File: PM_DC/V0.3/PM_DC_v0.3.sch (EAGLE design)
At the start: 49 parts, among them J1 M13PTH-CST-R, J2 M12PTH-CST-R, U2 LMR14030, U3 MP1601GTF-Z, U5 TPS22918

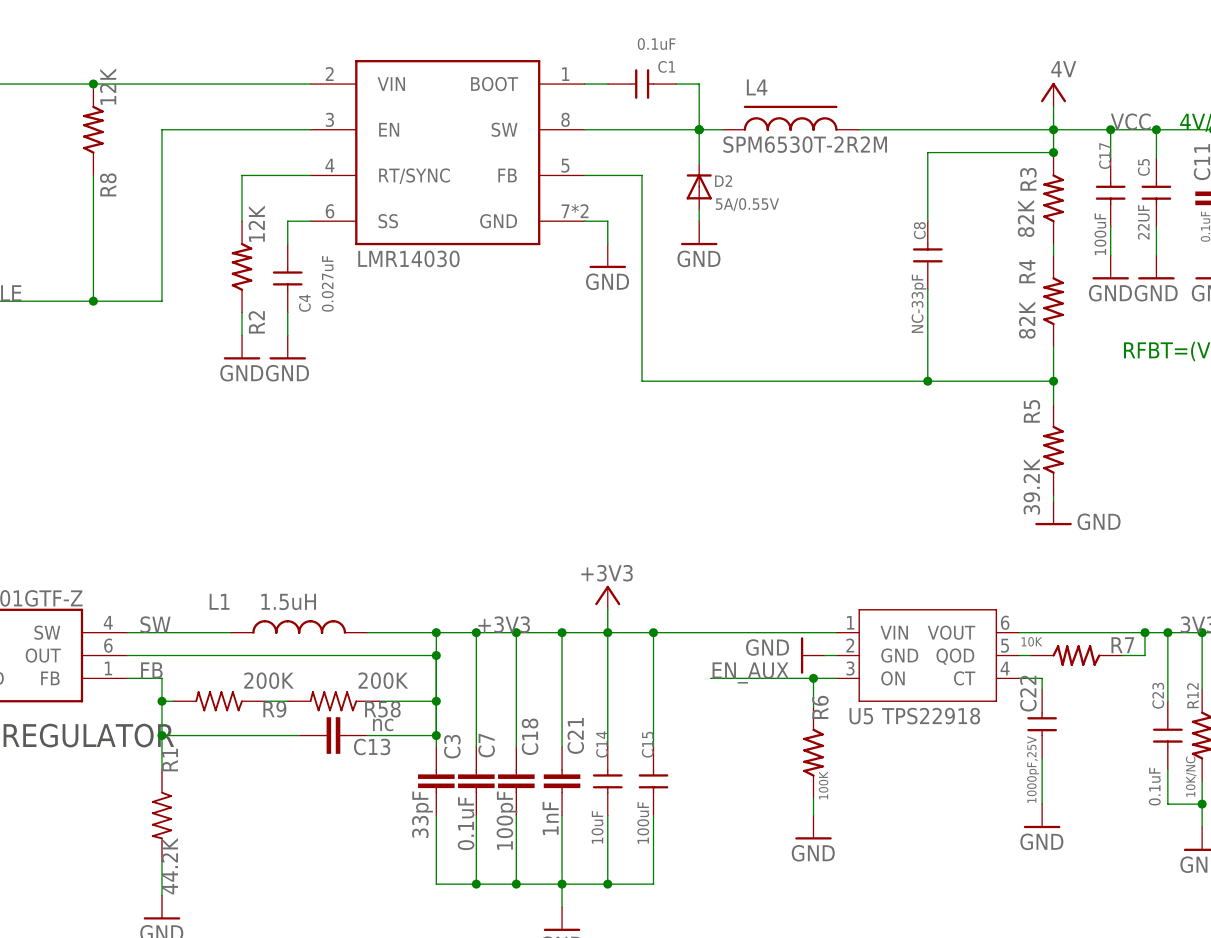
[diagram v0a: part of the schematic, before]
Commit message: update
output gerber for MO DFM
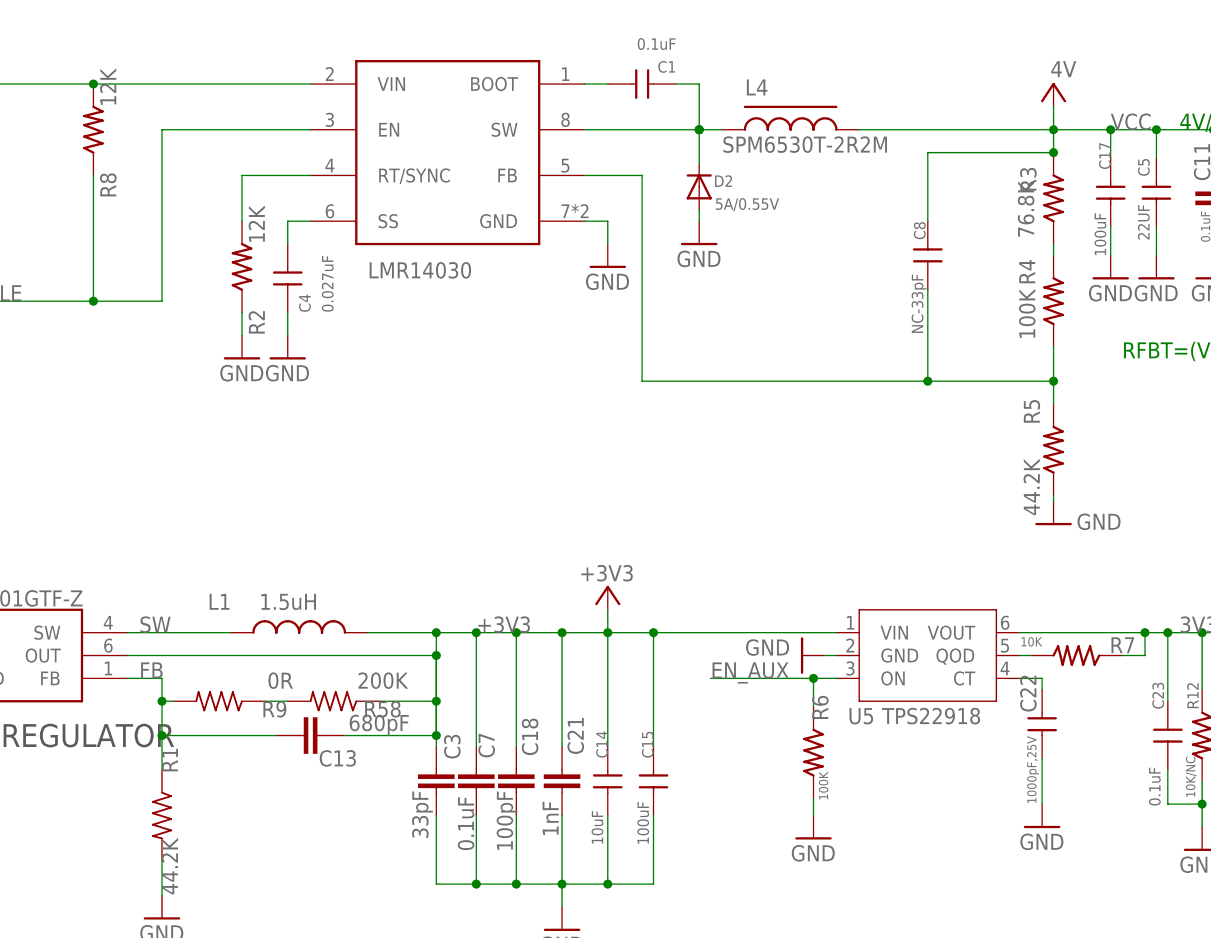
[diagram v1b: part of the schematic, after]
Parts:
- C13: value nc -> 680pF
- R3: value 82K -> 76.8K
- R4: value 82K -> 100K
- R5: value 39.2K -> 44.2K
- R9: value 200K -> 0R
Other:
- moved on the sheet: C13
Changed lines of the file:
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@@
 <part name="C1" library="particle SZ" library_urn="urn:adsk.eagle:library:21650216" deviceset="CAP" device="0402A" package3d_urn="urn:adsk.eagle:package:21650778/5" value="0.1uF"/>
 <part name="C8" library="particle SZ" library_urn="urn:adsk.eagle:library:21650216" deviceset="CAP" device="0402A" package3d_urn="urn:adsk.eagle:package:21650778/5" value="NC-33pF"/>
-<part name="R3" library="particle SZ" library_urn="urn:adsk.eagle:library:21650216" deviceset="RES" device="0402S" package3d_urn="urn:adsk.eagle:package:21650840/5" value="82K"/>
-<part name="R4" library="particle SZ" library_urn="urn:adsk.eagle:library:21650216" deviceset="RES" device="0402S" package3d_urn="urn:adsk.eagle:package:21650840/5" value="82K"/>
-<part name="R5" library="particle SZ" library_urn="urn:adsk.eagle:library:21650216" deviceset="RES" device="0402S" package3d_urn="urn:adsk.eagle:package:21650840/5" value="39.2K"/>
+<part name="R3" library="particle SZ" library_urn="urn:adsk.eagle:library:21650216" deviceset="RES" device="0402S" package3d_urn="urn:adsk.eagle:package:21650840/5" value="76.8K"/>
+<part name="R4" library="particle SZ" library_urn="urn:adsk.eagle:library:21650216" deviceset="RES" device="0402S" package3d_urn="urn:adsk.eagle:package:21650840/5" value="100K"/>
+<part name="R5" library="particle SZ" library_urn="urn:adsk.eagle:library:21650216" deviceset="RES" device="0402S" package3d_urn="urn:adsk.eagle:package:21650840/5" value="44.2K"/>
 <part name="C9" library="Particle" deviceset="CAP_1" device="" value="0.1uF"/>
 <part name="C10" library="Particle" deviceset="CAP_1" device="" value="1000pF"/>
 <part name="C11" library="Particle" deviceset="CAP_1" device="" value="0.1uF"/>
 <part name="C12" library="Particle" deviceset="CAP_1" device="" value="1000pF"/>
-<part name="C13" library="Particle" deviceset="CAP_1" device="" value="nc"/>
+<part name="C13" library="Particle" deviceset="CAP_1" device="" value="680pF"/>
 <part name="C14" library="particle SZ" deviceset="CAP" device="C0805" value="10uF"/>
 <part name="C5" library="particle SZ" deviceset="CAP" device="C0805" value="22UF"/>
@@
 <attribute name="ITEM_NUMBER" value=""/>
 </part>
-<part name="R9" library="Particle" deviceset="R-US_" device="" value="200K"/>
+<part name="R9" library="Particle" deviceset="R-US_" device="" value="0R"/>
 </parts>
 <sheets>
@@
 </instance>
 <instance part="U2" gate="G$1" x="154.94" y="132.08" smashed="yes">
-<attribute name="VALUE" x="144.78" y="119.38" size="1.778" layer="96"/>
+<attribute name="VALUE" x="146.05" y="118.11" size="1.778" layer="96"/>
 </instance>
 <instance part="GND22" gate="1" x="137.16" y="109.22" smashed="yes">
@@
 <attribute name="VALUE" x="243.586" y="125.73" size="1.016" layer="96" rot="R270"/>
 </instance>
-<instance part="C13" gate="G$1" x="142.24" y="67.31" smashed="yes" rot="R270">
-<attribute name="NAME" x="144.399" y="65.151" size="1.778" layer="95"/>
-<attribute name="VALUE" x="146.431" y="67.818" size="1.778" layer="96"/>
+<instance part="C13" gate="G$1" x="139.7" y="67.31" smashed="yes" rot="R270">
+<attribute name="NAME" x="140.589" y="63.881" size="1.778" layer="95"/>
+<attribute name="VALUE" x="143.891" y="67.818" size="1.778" layer="96"/>
 </instance>
 <instance part="C14" gate="G$1" x="172.72" y="60.96" smashed="yes">
@@
 <pinref part="C13" gate="G$1" pin="P$1"/>
 <pinref part="C14" gate="G$1" pin="1"/>
-<wire x1="146.05" y1="67.31" x2="153.67" y2="67.31" width="0.1524" layer="91"/>
+<wire x1="143.51" y1="67.31" x2="153.67" y2="67.31" width="0.1524" layer="91"/>
 <wire x1="153.67" y1="66.04" x2="153.67" y2="67.31" width="0.1524" layer="91"/>
 <wire x1="172.72" y1="78.74" x2="177.8" y2="78.74" width="0.1524" layer="91"/>
@@
 <junction x="123.19" y="71.12"/>
 <pinref part="C13" gate="G$1" pin="P$2"/>
-<wire x1="138.43" y1="67.31" x2="123.19" y2="67.31" width="0.1524" layer="91"/>
+<wire x1="135.89" y1="67.31" x2="123.19" y2="67.31" width="0.1524" layer="91"/>
 <junction x="123.19" y="67.31"/>
 </segment>
